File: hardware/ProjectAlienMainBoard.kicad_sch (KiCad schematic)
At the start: 15 parts, among them J1 Bumper Connector, J3 Left Motor Connector, J4 Right Motor Connector, J5 Pixels Connector, J6 Ultrasonic Connector, J7 Micro USB, J8 I2C Multiplexer, U1 4021

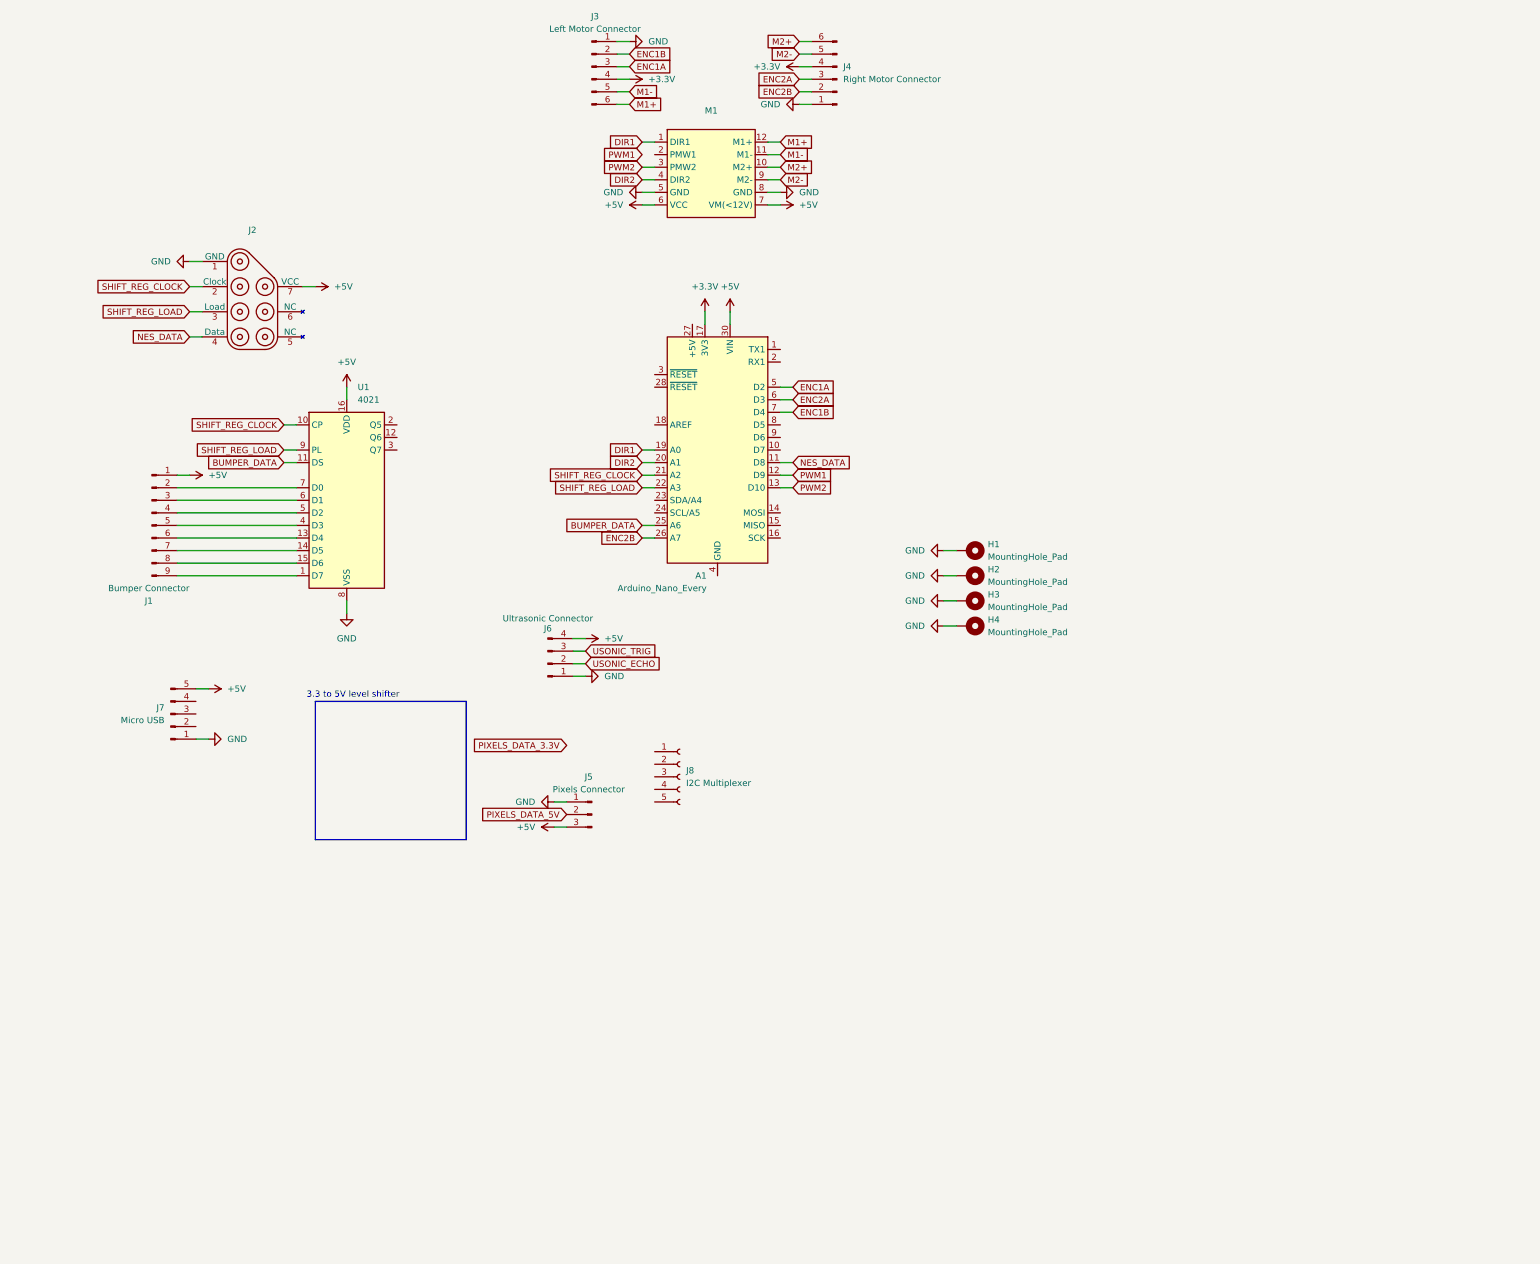
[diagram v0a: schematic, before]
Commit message: Swapped resistors for SMT
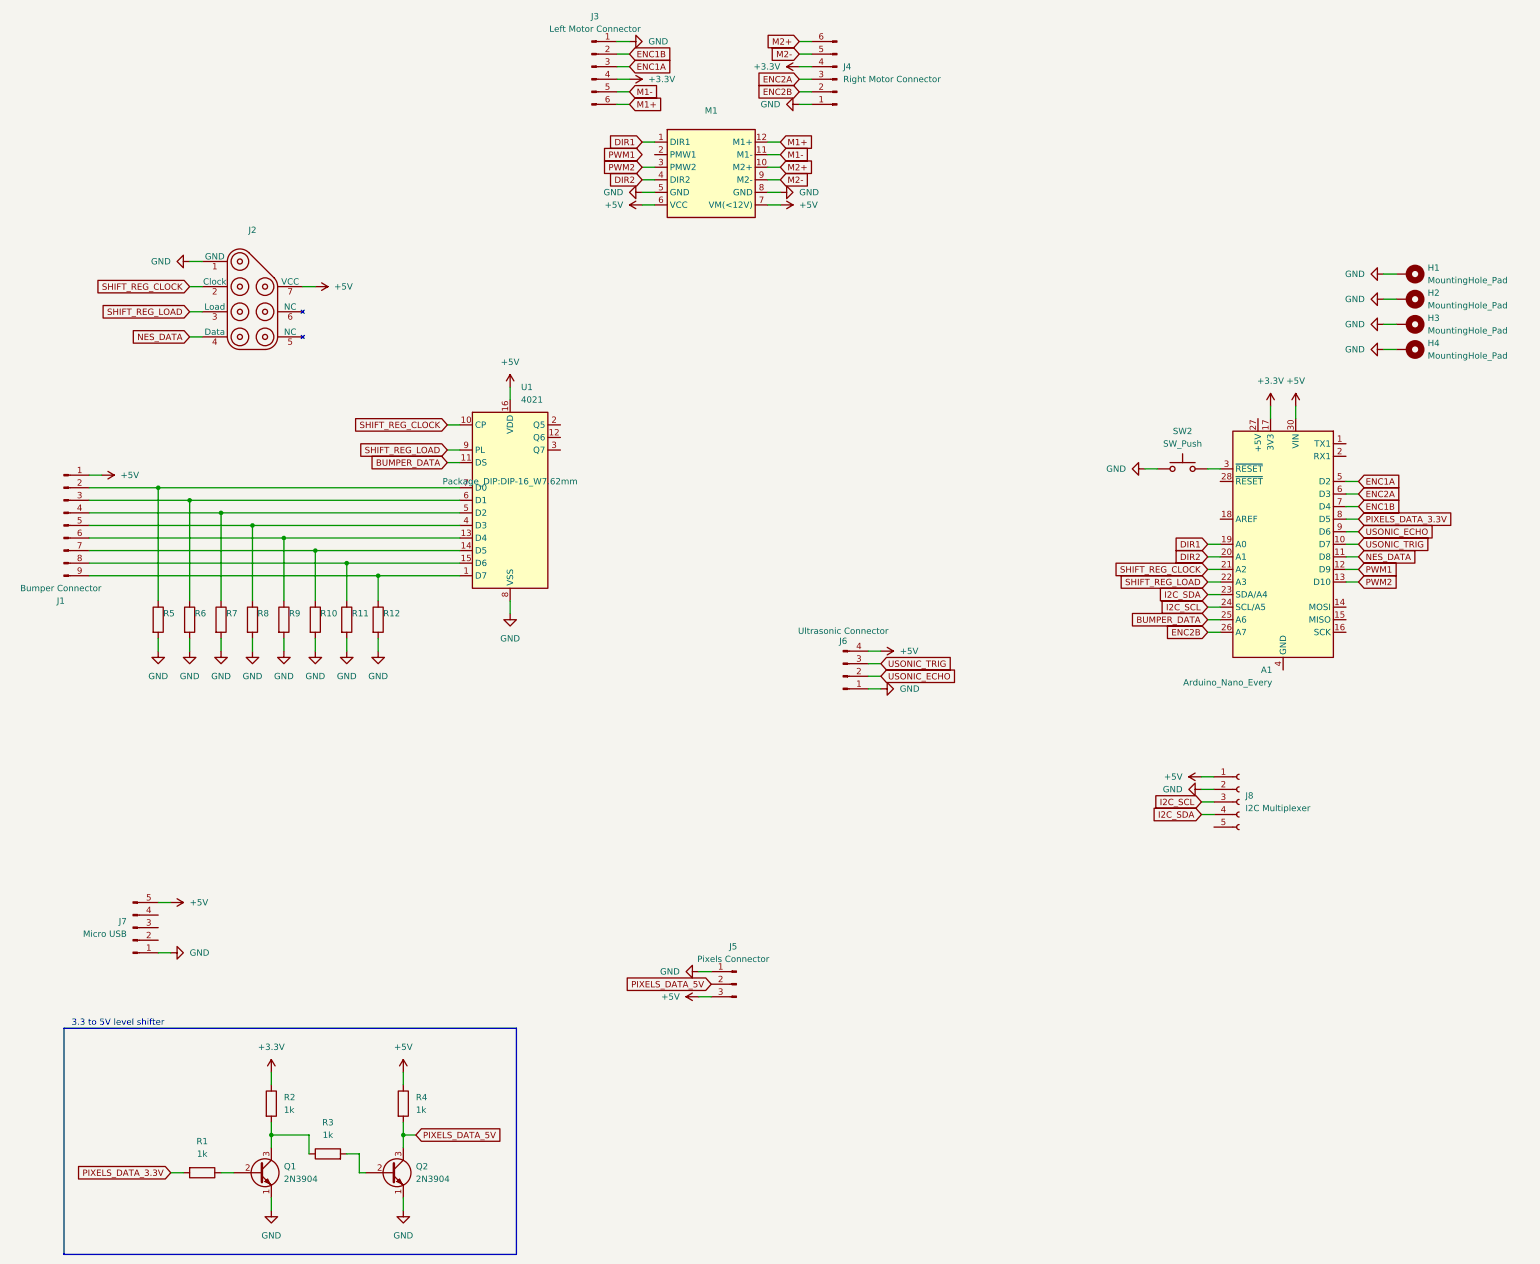
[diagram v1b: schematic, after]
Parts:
- added Q1, Q2: 2N3904, Package_TO_SOT_THT:TO-92_Inline, symbol Transistor_BJT:2N3904
- added R1, R2, R3, R4: 1k, Resistor_SMD:R_0402_1005Metric_Pad0.72x0.64mm_HandSolder, symbol Device:R
- added R10, R11, R12, R5, R6, R7, R8, R9: 10k, Resistor_SMD:R_0402_1005Metric_Pad0.72x0.64mm_HandSolder, symbol Device:R
- added SW2: SW_Push, Two_Pin_Through_Hole_Push_Button:Two_Pin_Through_Hole_Push_Button, symbol Switch:SW_Push
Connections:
- net +3.3V: now also R2.1
- net +5V: now also J8.1 (Pin_1), R4.1
- net GND: now also J8.2 (Pin_2), Q1.1 (E), Q2.1 (E), R10.2, R11.2, R12.2, R5.2, R6.2, R7.2, R8.2, R9.2, SW2.1
- net PIXELS_DATA_3.3V: now also A1.8 (D5), R1.2
- net PIXELS_DATA_5V: now also Q2.3 (C), R4.2
- net USONIC_ECHO: now also A1.9 (D6)
- net USONIC_TRIG: now also A1.10 (D7)
- net at J1.9 (Pin_9), U1.1 (D7): now also R12.1
- net at J1.6 (Pin_6), U1.13 (D4): now also R9.1
- net at J1.7 (Pin_7), U1.14 (D5): now also R10.1
- net at J1.8 (Pin_8), U1.15 (D6): now also R11.1
- net at J1.5 (Pin_5), U1.4 (D3): now also R8.1
- net at J1.4 (Pin_4), U1.5 (D2): now also R7.1
- net at J1.3 (Pin_3), U1.6 (D1): now also R6.1
- net at J1.2 (Pin_2), U1.7 (D0): now also R5.1
- net I2C_SDA: now reaches A1.23 (SDA/A4)
- net I2C_SDA: now also J8.4 (Pin_4)
- net I2C_SCL: now reaches A1.24 (SCL/A5)
- net I2C_SCL: now also J8.3 (Pin_3)
- net at A1.3 (~{RESET}): now also SW2.2
- new net: Q1.2 (B), R1.1
- new net: Q2.2 (B), R3.2
- new net: Q1.3 (C), R2.2, R3.1
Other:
- moved on the sheet: A1, H1, H2, H3, H4, J1, J5, J6, J7, J8, U1

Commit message: Routed Tracks
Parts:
- added GND1: GND, TestPoint:TestPoint_Bridge_Pitch2.54mm_Drill0.7mm, symbol Connector:TestPoint
- added J98: Voltage Breakout, Connector_PinHeader_2.54mm:PinHeader_1x03_P2.54mm_Vertical, symbol Connector:Conn_01x03_Pin
- added J99: Excess GPIO Pins, Connector_PinHeader_2.54mm:PinHeader_1x03_P2.54mm_Vertical, symbol Connector:Conn_01x03_Pin
- added TP1, TP10, TP11, TP12, TP13, TP14, TP15, TP16, TP17, TP18, TP19, TP2, TP20, TP3, TP4, TP5, TP6, TP7, TP8, TP9: TestPoint, TestPoint:TestPoint_THTPad_D1.0mm_Drill0.5mm, symbol Connector:TestPoint
- A1: value Arduino_Nano_Every -> Arduino_Nano_33_BLE
- SW1: renamed from SW2; value SW_Push -> Reset Button
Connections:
- net +3.3V: now also J1.1 (Pin_1), J2.7 (VCC), U1.16 (VDD), J98.2 (Pin_2)
- net +5V: now also J98.3 (Pin_3); no longer J1.1 (Pin_1), J2.7 (VCC), U1.16 (VDD)
- net BUMPER_DATA: now also TP6.1
- net DIR1: now also TP9.1
- net DIR2: now also TP12.1
- net ENC1A: now also TP17.1
- net ENC1B: now also TP18.1
- net ENC2A: now also TP19.1
- net ENC2B: now also TP20.1
- net GND: now also A1.29 (GND), A1.4 (GND), GND1.1, J98.1 (Pin_1)
- net M1+: now also TP13.1
- net M1-: now also TP14.1
- net M2+: now also TP15.1
- net M2-: now also TP16.1
- net NES_DATA: now also TP5.1
- net PIXELS_DATA_3.3V: now also TP3.1
- net PIXELS_DATA_5V: now also TP4.1
- net PWM1: now also M1.2 (PMW1), TP10.1
- net PWM2: now also TP11.1
- net SHIFT_REG_CLOCK: now also TP8.1
- net SHIFT_REG_LOAD: now also TP7.1
- net USONIC_ECHO: now also TP1.1
- net USONIC_TRIG: now also TP2.1
- net Buzzer: now reaches A1.14 (MOSI)
- net D12: now reaches A1.15 (MISO)
- net D12: now also J99.2 (Pin_2)
- net D13: now reaches A1.16 (SCK)
- net D13: now also J99.3 (Pin_3)
- new net D11: J99.1 (Pin_1)
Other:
- moved on the sheet: U1

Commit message: Added ground plane
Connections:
- net Buzzer is gone; now on net D11: A1.14 (MOSI)
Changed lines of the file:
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@@
 		)
 	)
-	(global_label "Buzzer"
+	(global_label "D11"
 		(shape input)
 		(at 283.21 142.24 0)
@@
 		)
 		(property "Intersheetrefs" "${INTERSHEET_REFS}"
-			(at 292.5452 142.24 0)
+			(at 289.8842 142.24 0)
 			(effects
 				(font

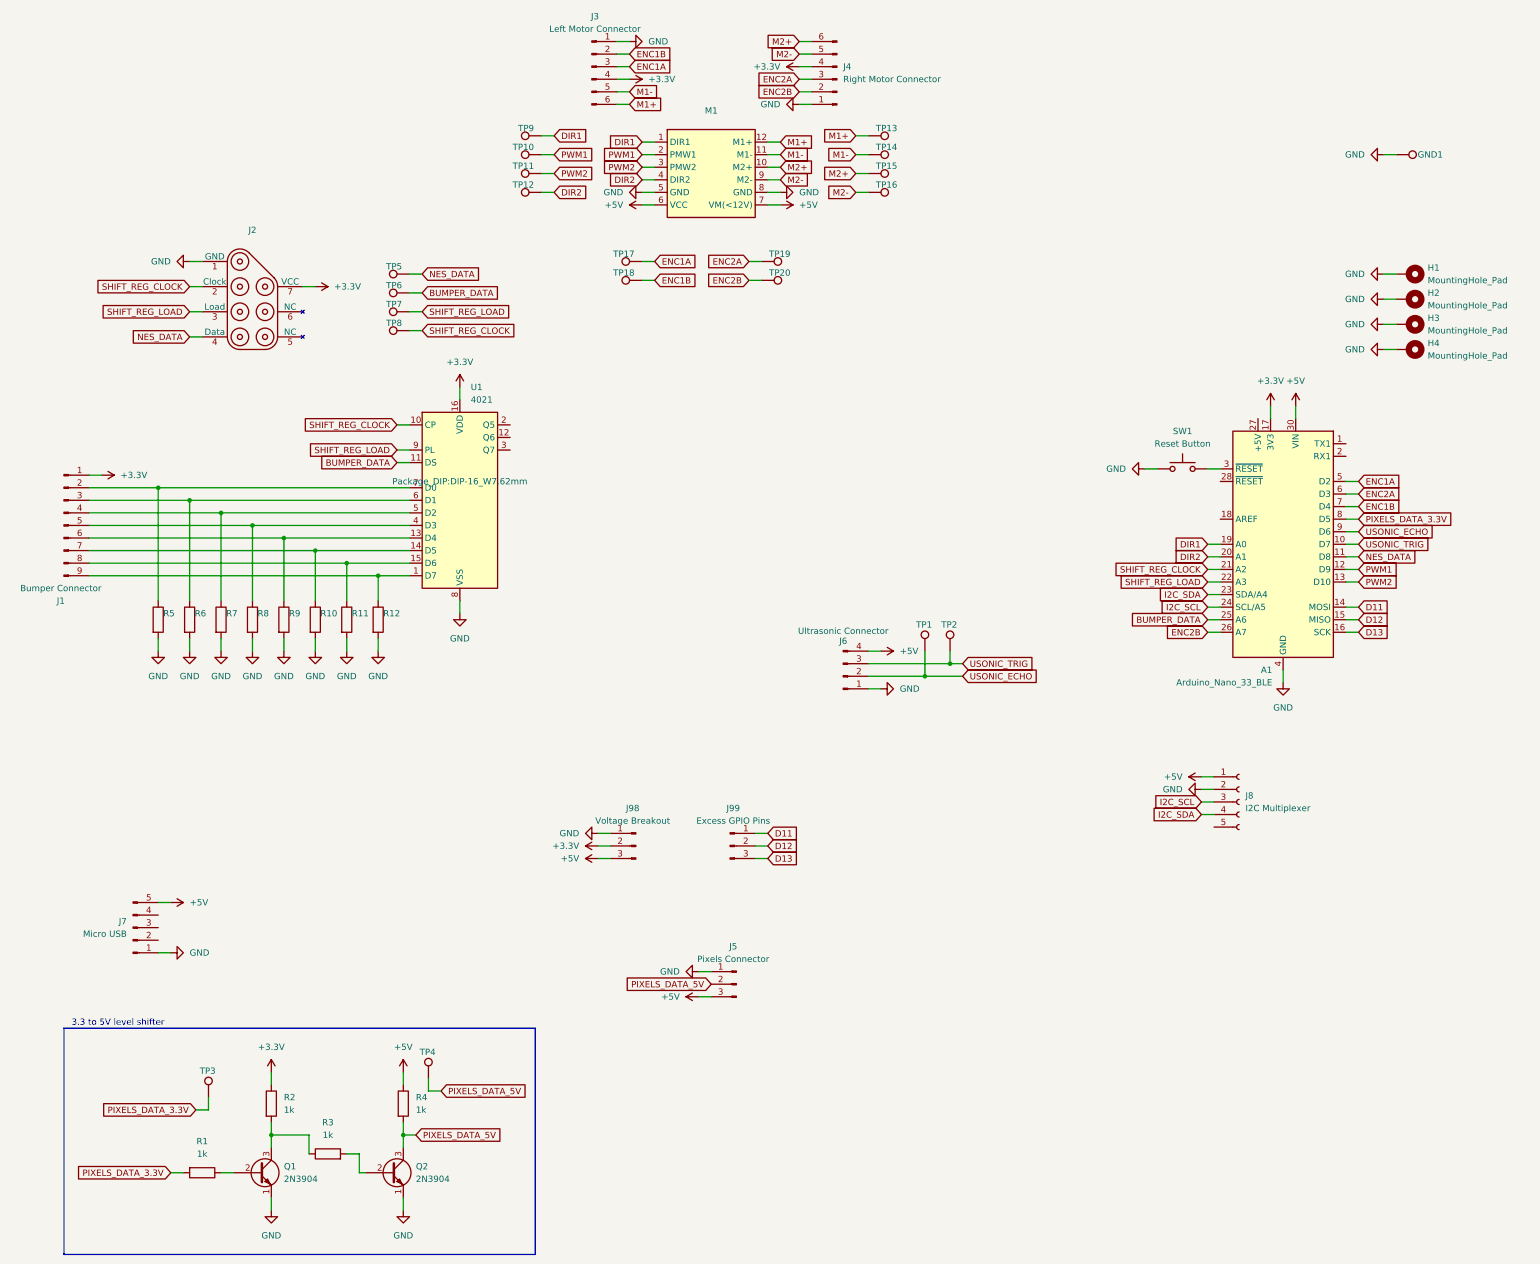
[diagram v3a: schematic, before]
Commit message: Finished component silkscreen labels
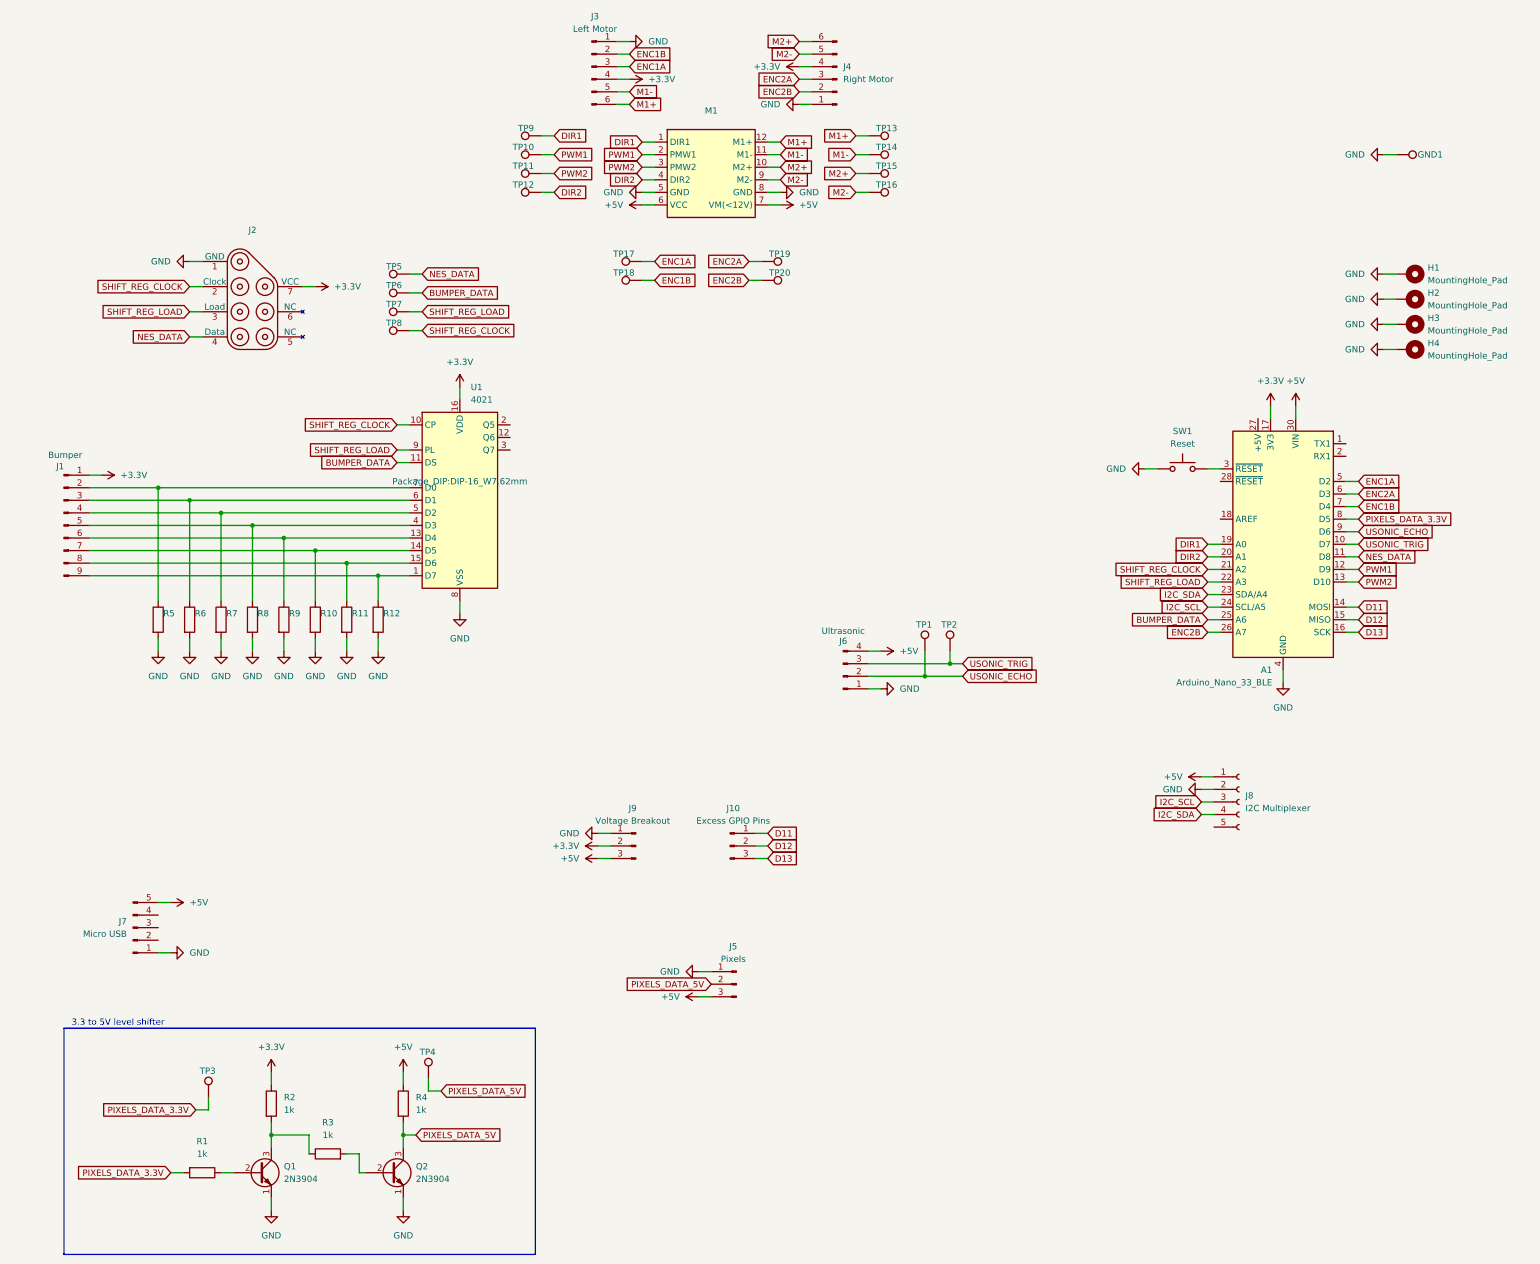
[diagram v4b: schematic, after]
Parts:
- J1: value Bumper Connector -> Bumper
- J3: value Left Motor Connector -> Left Motor
- J4: value Right Motor Connector -> Right Motor
- J5: value Pixels Connector -> Pixels
- J6: value Ultrasonic Connector -> Ultrasonic
- SW1: value Reset Button -> Reset
- renumbered J99 to J10, J98 to J9
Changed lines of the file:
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@@
 			)
 		)
-		(property "Value" "Right Motor Connector"
+		(property "Value" "Right Motor"
 			(at 179.07 35.5599 0)
 			(effects
@@
 			)
 		)
-		(property "Value" "Left Motor Connector"
+		(property "Value" "Left Motor"
 			(at 128.905 25.4 0)
 			(effects
@@
 			)
 		)
-		(property "Value" "Pixels Connector"
+		(property "Value" "Pixels"
 			(at 156.845 213.36 0)
 			(effects
@@
 			)
 		)
-		(property "Value" "Ultrasonic Connector"
+		(property "Value" "Ultrasonic"
 			(at 179.07 147.066 0)
 			(effects
@@
 		(on_board yes)
 		(dnp no)
-		(property "Reference" "J98"
+		(property "Reference" "J9"
 			(at 136.525 182.88 0)
 			(effects
@@
 			(project "ProjectAlienMainBoard"
 				(path "/170b00d5-17da-40d3-a37d-b29c3db0afc1"
-					(reference "J98")
+					(reference "J9")
 					(unit 1)
 				)
@@
 		(dnp no)
 		(property "Reference" "J1"
-			(at 20.955 140.97 0)
+			(at 20.828 113.792 0)
 			(effects
 				(font
@@
 			)
 		)
-		(property "Value" "Bumper Connector"
-			(at 20.955 138.43 0)
+		(property "Value" "Bumper "
+			(at 21.844 111.506 0)
 			(effects
 				(font
@@
 			)
 		)
-		(property "Value" "Reset Button"
+		(property "Value" "Reset"
 			(at 247.65 109.22 0)
 			(effects
@@
 		(on_board yes)
 		(dnp no)
-		(property "Reference" "J99"
+		(property "Reference" "J10"
 			(at 156.845 182.88 0)
 			(effects
@@
 			(project "ProjectAlienMainBoard"
 				(path "/170b00d5-17da-40d3-a37d-b29c3db0afc1"
-					(reference "J99")
+					(reference "J10")
 					(unit 1)
 				)
